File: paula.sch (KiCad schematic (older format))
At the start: 79 parts, among them CN200 DB9P RIGHT(1), CN201 DB9P LEFT(0), CN204 RIGHT AUDIO, CN205 LEFT AUDIO, J200 Conn_01x03_Male, Q200 MPF102, Q201 MPF102, Q202 2N3906, U200 PAULA, U202 74LS157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

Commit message: Makes the DRC happy
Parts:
- EMI230, EMI231, EMI232, EMI233, EMI234, EMI235, EMI236, EMI237, EMI238, EMI239, EMI240, EMI241, EMI242, EMI243: footprint Connector_PinSocket_2.54mm:PinSocket_1x03_P2.54mm_Vertical -> d_amiga:EMI_FILTER
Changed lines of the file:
@@
 F 0 "EMI231" H 6450 7600 50  0000 C CNN
 F 1 "C_Feedthrough" H 6350 7814 50  0001 C CNN
-F 2 "Connector_PinSocket_2.54mm:PinSocket_1x03_P2.54mm_Vertical" V 6350 7600 50  0001 C CNN
+F 2 "d_amiga:EMI_FILTER" V 6350 7600 50  0001 C CNN
 F 3 "~" V 6350 7600 50  0001 C CNN
 	1    6350 7600
@@
 F 0 "EMI232" H 6800 7800 50  0000 C CNN
 F 1 "C_Feedthrough" H 6700 8014 50  0001 C CNN
-F 2 "Connector_PinSocket_2.54mm:PinSocket_1x03_P2.54mm_Vertical" V 6700 7800 50  0001 C CNN
+F 2 "d_amiga:EMI_FILTER" V 6700 7800 50  0001 C CNN
 F 3 "~" V 6700 7800 50  0001 C CNN
 	1    6700 7800
@@
 F 0 "EMI233" H 7200 8000 50  0000 C CNN
 F 1 "C_Feedthrough" H 7100 8214 50  0001 C CNN
-F 2 "Connector_PinSocket_2.54mm:PinSocket_1x03_P2.54mm_Vertical" V 7100 8000 50  0001 C CNN
+F 2 "d_amiga:EMI_FILTER" V 7100 8000 50  0001 C CNN
 F 3 "~" V 7100 8000 50  0001 C CNN
 	1    7100 8000
@@
 F 0 "EMI230" H 6050 7400 50  0000 C CNN
 F 1 "C_Feedthrough" H 5950 7614 50  0001 C CNN
-F 2 "Connector_PinSocket_2.54mm:PinSocket_1x03_P2.54mm_Vertical" V 5950 7400 50  0001 C CNN
+F 2 "d_amiga:EMI_FILTER" V 5950 7400 50  0001 C CNN
 F 3 "~" V 5950 7400 50  0001 C CNN
 	1    5950 7400
@@
 F 0 "EMI234" H 6050 9600 50  0000 C CNN
 F 1 "C_Feedthrough" H 5950 9814 50  0001 C CNN
-F 2 "Connector_PinSocket_2.54mm:PinSocket_1x03_P2.54mm_Vertical" V 5950 9600 50  0001 C CNN
+F 2 "d_amiga:EMI_FILTER" V 5950 9600 50  0001 C CNN
 F 3 "~" V 5950 9600 50  0001 C CNN
 	1    5950 9600
@@
 F 0 "EMI235" H 6450 9800 50  0000 C CNN
 F 1 "C_Feedthrough" H 6350 10014 50  0001 C CNN
-F 2 "Connector_PinSocket_2.54mm:PinSocket_1x03_P2.54mm_Vertical" V 6350 9800 50  0001 C CNN
+F 2 "d_amiga:EMI_FILTER" V 6350 9800 50  0001 C CNN
 F 3 "~" V 6350 9800 50  0001 C CNN
 	1    6350 9800
@@
 F 0 "EMI236" H 6850 10000 50  0000 C CNN
 F 1 "C_Feedthrough" H 6750 10214 50  0001 C CNN
-F 2 "Connector_PinSocket_2.54mm:PinSocket_1x03_P2.54mm_Vertical" V 6750 10000 50  0001 C CNN
+F 2 "d_amiga:EMI_FILTER" V 6750 10000 50  0001 C CNN
 F 3 "~" V 6750 10000 50  0001 C CNN
 	1    6750 10000
@@
 F 0 "EMI237" H 7250 10200 50  0000 C CNN
 F 1 "C_Feedthrough" H 7150 10414 50  0001 C CNN
-F 2 "Connector_PinSocket_2.54mm:PinSocket_1x03_P2.54mm_Vertical" V 7150 10200 50  0001 C CNN
+F 2 "d_amiga:EMI_FILTER" V 7150 10200 50  0001 C CNN
 F 3 "~" V 7150 10200 50  0001 C CNN
 	1    7150 10200
@@
 F 0 "EMI238" H 9300 7100 50  0000 C CNN
 F 1 "C_Feedthrough" H 9200 7314 50  0001 C CNN
-F 2 "Connector_PinSocket_2.54mm:PinSocket_1x03_P2.54mm_Vertical" V 9200 7100 50  0001 C CNN
+F 2 "d_amiga:EMI_FILTER" V 9200 7100 50  0001 C CNN
 F 3 "~" V 9200 7100 50  0001 C CNN
 	1    9200 7100
@@
 F 0 "EMI239" H 9300 8400 50  0000 C CNN
 F 1 "C_Feedthrough" H 9200 8614 50  0001 C CNN
-F 2 "Connector_PinSocket_2.54mm:PinSocket_1x03_P2.54mm_Vertical" V 9200 8400 50  0001 C CNN
+F 2 "d_amiga:EMI_FILTER" V 9200 8400 50  0001 C CNN
 F 3 "~" V 9200 8400 50  0001 C CNN
 	1    9200 8400
@@
 F 0 "EMI240" H 9300 8750 50  0000 C CNN
 F 1 "C_Feedthrough" H 9200 8964 50  0001 C CNN
-F 2 "Connector_PinSocket_2.54mm:PinSocket_1x03_P2.54mm_Vertical" V 9200 8750 50  0001 C CNN
+F 2 "d_amiga:EMI_FILTER" V 9200 8750 50  0001 C CNN
 F 3 "~" V 9200 8750 50  0001 C CNN
 	1    9200 8750
@@
 F 0 "EMI241" H 9300 9350 50  0000 C CNN
 F 1 "C_Feedthrough" H 9200 9564 50  0001 C CNN
-F 2 "Connector_PinSocket_2.54mm:PinSocket_1x03_P2.54mm_Vertical" V 9200 9350 50  0001 C CNN
+F 2 "d_amiga:EMI_FILTER" V 9200 9350 50  0001 C CNN
 F 3 "~" V 9200 9350 50  0001 C CNN
 	1    9200 9350
@@
 F 0 "EMI242" H 9300 10600 50  0000 C CNN
 F 1 "C_Feedthrough" H 9200 10814 50  0001 C CNN
-F 2 "Connector_PinSocket_2.54mm:PinSocket_1x03_P2.54mm_Vertical" V 9200 10600 50  0001 C CNN
+F 2 "d_amiga:EMI_FILTER" V 9200 10600 50  0001 C CNN
 F 3 "~" V 9200 10600 50  0001 C CNN
 	1    9200 10600
@@
 F 0 "EMI243" H 9300 10900 50  0000 C CNN
 F 1 "C_Feedthrough" H 9200 11114 50  0001 C CNN
-F 2 "Connector_PinSocket_2.54mm:PinSocket_1x03_P2.54mm_Vertical" V 9200 10900 50  0001 C CNN
+F 2 "d_amiga:EMI_FILTER" V 9200 10900 50  0001 C CNN
 F 3 "~" V 9200 10900 50  0001 C CNN
 	1    9200 10900

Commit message: Add DoNotPopulate field for components which shouldn't be fitted
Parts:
- C230, C240: DoNotPopulate (none) -> yes
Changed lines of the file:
@@
 F 2 "Capacitor_THT:C_Rect_L11.5mm_W2.0mm_P10.00mm_MKT" H 6588 1200 50  0001 C CNN
 F 3 "~" H 6550 1350 50  0001 C CNN
+F 4 "yes" H 6550 1350 50  0001 C CNN "DoNotPopulate"
 	1    6550 1350
 	1    0    0    -1
@@
 F 2 "Capacitor_THT:C_Rect_L11.5mm_W2.0mm_P10.00mm_MKT" H 6588 3350 50  0001 C CNN
 F 3 "~" H 6550 3500 50  0001 C CNN
+F 4 "yes" H 6550 3500 50  0001 C CNN "DoNotPopulate"
 	1    6550 3500
 	1    0    0    -1

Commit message: Switch footprints for suitable modern replacements
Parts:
- C200, C202, C210, C211, C212, C213, C218, C230, C231, C232, C234, C240, C241, C242, C244, C900, C901: footprint Capacitor_THT:C_Rect_L11.5mm_W2.0mm_P10.00mm_MKT -> Capacitor_THT:C_Rect_L11.5mm_W2.6mm_P10.00mm_MKT
- C219, C220, C221: footprint Capacitor_THT:C_Rect_L11.5mm_W2.0mm_P10.00mm_MKT -> Capacitor_THT:C_Rect_L11.5mm_W4.0mm_P10.00mm_MKT
- C224: footprint Capacitor_THT:CP_Radial_D8.0mm_P5.00mm -> Capacitor_THT:CP_Radial_D5.0mm_P2.50mm
- C225: value 470uF 16v -> 470uF 16/25v
- C233: footprint Capacitor_THT:CP_Radial_D6.3mm_P2.50mm -> Capacitor_THT:CP_Radial_D8.0mm_P5.00mm
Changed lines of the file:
@@
 P 2750 750
 F 0 "C225" V 2900 700 50  0000 C CNN
-F 1 "470uF 16v" V 2800 500 50  0000 C CNN
+F 1 "470uF 16/25v" V 2800 500 50  0000 C CNN
 F 2 "Capacitor_THT:CP_Radial_D10.0mm_P5.00mm" H 2788 600 50  0001 C CNN
 F 3 "~" H 2750 750 50  0001 C CNN
@@
 F 0 "C200" V 2350 950 50  0000 C CNN
 F 1 "0.1uF" V 2650 950 50  0000 C CNN
-F 2 "Capacitor_THT:C_Rect_L11.5mm_W2.0mm_P10.00mm_MKT" H 2538 800 50  0001 C CNN
+F 2 "Capacitor_THT:C_Rect_L11.5mm_W2.6mm_P10.00mm_MKT" H 2538 800 50  0001 C CNN
 F 3 "~" H 2500 950 50  0001 C CNN
 	1    2500 950
@@
 F 0 "C210" H 3915 6046 50  0000 L CNN
 F 1 "0.047uF" H 3915 5955 50  0000 L CNN
-F 2 "Capacitor_THT:C_Rect_L11.5mm_W2.0mm_P10.00mm_MKT" H 3838 5850 50  0001 C CNN
+F 2 "Capacitor_THT:C_Rect_L11.5mm_W2.6mm_P10.00mm_MKT" H 3838 5850 50  0001 C CNN
 F 3 "~" H 3800 6000 50  0001 C CNN
 	1    3800 6000
@@
 F 0 "C211" H 4465 6046 50  0000 L CNN
 F 1 "0.047uF" H 4465 5955 50  0000 L CNN
-F 2 "Capacitor_THT:C_Rect_L11.5mm_W2.0mm_P10.00mm_MKT" H 4388 5850 50  0001 C CNN
+F 2 "Capacitor_THT:C_Rect_L11.5mm_W2.6mm_P10.00mm_MKT" H 4388 5850 50  0001 C CNN
 F 3 "~" H 4350 6000 50  0001 C CNN
 	1    4350 6000
@@
 F 0 "C212" H 5015 6046 50  0000 L CNN
 F 1 "0.047uF" H 5015 5955 50  0000 L CNN
-F 2 "Capacitor_THT:C_Rect_L11.5mm_W2.0mm_P10.00mm_MKT" H 4938 5850 50  0001 C CNN
+F 2 "Capacitor_THT:C_Rect_L11.5mm_W2.6mm_P10.00mm_MKT" H 4938 5850 50  0001 C CNN
 F 3 "~" H 4900 6000 50  0001 C CNN
 	1    4900 6000
@@
 F 0 "C213" H 5565 6046 50  0000 L CNN
 F 1 "0.047uF" H 5565 5955 50  0000 L CNN
-F 2 "Capacitor_THT:C_Rect_L11.5mm_W2.0mm_P10.00mm_MKT" H 5488 5850 50  0001 C CNN
+F 2 "Capacitor_THT:C_Rect_L11.5mm_W2.6mm_P10.00mm_MKT" H 5488 5850 50  0001 C CNN
 F 3 "~" H 5450 6000 50  0001 C CNN
 	1    5450 6000
@@
 F 0 "C218" V 6721 6750 50  0000 C CNN
 F 1 "0.047uF" V 6812 6750 50  0000 C CNN
-F 2 "Capacitor_THT:C_Rect_L11.5mm_W2.0mm_P10.00mm_MKT" H 6950 6750 50  0001 C CNN
+F 2 "Capacitor_THT:C_Rect_L11.5mm_W2.6mm_P10.00mm_MKT" H 6950 6750 50  0001 C CNN
 F 3 "~" H 6950 6750 50  0001 C CNN
 	1    6950 6750
@@
 F 0 "C202" H 3315 8646 50  0000 L CNN
 F 1 "0.1uF" H 3315 8555 50  0000 L CNN
-F 2 "Capacitor_THT:C_Rect_L11.5mm_W2.0mm_P10.00mm_MKT" H 3238 8450 50  0001 C CNN
+F 2 "Capacitor_THT:C_Rect_L11.5mm_W2.6mm_P10.00mm_MKT" H 3238 8450 50  0001 C CNN
 F 3 "~" H 3200 8600 50  0001 C CNN
 	1    3200 8600
@@
 F 0 "C220" H 10715 7346 50  0000 L CNN
 F 1 "0.22uF" H 10715 7255 50  0000 L CNN
-F 2 "Capacitor_THT:C_Rect_L11.5mm_W2.0mm_P10.00mm_MKT" H 10638 7150 50  0001 C CNN
+F 2 "Capacitor_THT:C_Rect_L11.5mm_W4.0mm_P10.00mm_MKT" H 10638 7150 50  0001 C CNN
 F 3 "~" H 10600 7300 50  0001 C CNN
 	1    10600 7300
@@
 F 0 "C221" H 10715 7846 50  0000 L CNN
 F 1 "0.22uF" H 10715 7755 50  0000 L CNN
-F 2 "Capacitor_THT:C_Rect_L11.5mm_W2.0mm_P10.00mm_MKT" H 10638 7650 50  0001 C CNN
+F 2 "Capacitor_THT:C_Rect_L11.5mm_W4.0mm_P10.00mm_MKT" H 10638 7650 50  0001 C CNN
 F 3 "~" H 10600 7800 50  0001 C CNN
 	1    10600 7800
@@
 F 0 "C240" H 6665 1396 50  0000 L CNN
 F 1 "0.1uF" H 6665 1305 50  0000 L CNN
-F 2 "Capacitor_THT:C_Rect_L11.5mm_W2.0mm_P10.00mm_MKT" H 6588 1200 50  0001 C CNN
+F 2 "Capacitor_THT:C_Rect_L11.5mm_W2.6mm_P10.00mm_MKT" H 6588 1200 50  0001 C CNN
 F 3 "~" H 6550 1350 50  0001 C CNN
 F 4 "yes" H 6550 1350 50  0001 C CNN "DoNotPopulate"
@@
 F 0 "C241" H 8465 1196 50  0000 L CNN
 F 1 "6800pF" H 8465 1105 50  0000 L CNN
-F 2 "Capacitor_THT:C_Rect_L11.5mm_W2.0mm_P10.00mm_MKT" H 8388 1000 50  0001 C CNN
+F 2 "Capacitor_THT:C_Rect_L11.5mm_W2.6mm_P10.00mm_MKT" H 8388 1000 50  0001 C CNN
 F 3 "~" H 8350 1150 50  0001 C CNN
 	1    8350 1150
@@
 F 0 "C242" H 9915 1846 50  0000 L CNN
 F 1 "3900pF" H 9915 1755 50  0000 L CNN
-F 2 "Capacitor_THT:C_Rect_L11.5mm_W2.0mm_P10.00mm_MKT" H 9838 1650 50  0001 C CNN
+F 2 "Capacitor_THT:C_Rect_L11.5mm_W2.6mm_P10.00mm_MKT" H 9838 1650 50  0001 C CNN
 F 3 "~" H 9800 1800 50  0001 C CNN
 	1    9800 1800
@@
 F 0 "C244" H 13615 1996 50  0000 L CNN
 F 1 "0.1uF" H 13615 1905 50  0000 L CNN
-F 2 "Capacitor_THT:C_Rect_L11.5mm_W2.0mm_P10.00mm_MKT" H 13538 1800 50  0001 C CNN
+F 2 "Capacitor_THT:C_Rect_L11.5mm_W2.6mm_P10.00mm_MKT" H 13538 1800 50  0001 C CNN
 F 3 "~" H 13500 1950 50  0001 C CNN
 	1    13500 1950
@@
 F 0 "C230" H 6665 3546 50  0000 L CNN
 F 1 "0.1uF" H 6665 3455 50  0000 L CNN
-F 2 "Capacitor_THT:C_Rect_L11.5mm_W2.0mm_P10.00mm_MKT" H 6588 3350 50  0001 C CNN
+F 2 "Capacitor_THT:C_Rect_L11.5mm_W2.6mm_P10.00mm_MKT" H 6588 3350 50  0001 C CNN
 F 3 "~" H 6550 3500 50  0001 C CNN
 F 4 "yes" H 6550 3500 50  0001 C CNN "DoNotPopulate"
@@
 F 0 "C231" H 8465 3346 50  0000 L CNN
 F 1 "6800pF" H 8465 3255 50  0000 L CNN
-F 2 "Capacitor_THT:C_Rect_L11.5mm_W2.0mm_P10.00mm_MKT" H 8388 3150 50  0001 C CNN
+F 2 "Capacitor_THT:C_Rect_L11.5mm_W2.6mm_P10.00mm_MKT" H 8388 3150 50  0001 C CNN
 F 3 "~" H 8350 3300 50  0001 C CNN
 	1    8350 3300
@@
 F 0 "C232" H 9915 3996 50  0000 L CNN
 F 1 "3900pF" H 9915 3905 50  0000 L CNN
-F 2 "Capacitor_THT:C_Rect_L11.5mm_W2.0mm_P10.00mm_MKT" H 9838 3800 50  0001 C CNN
+F 2 "Capacitor_THT:C_Rect_L11.5mm_W2.6mm_P10.00mm_MKT" H 9838 3800 50  0001 C CNN
 F 3 "~" H 9800 3950 50  0001 C CNN
 	1    9800 3950
@@
 F 0 "C233" V 12205 3850 50  0000 C CNN
 F 1 "22uF 16V" V 12114 3850 50  0000 C CNN
-F 2 "Capacitor_THT:CP_Radial_D6.3mm_P2.50mm" H 11988 3700 50  0001 C CNN
+F 2 "Capacitor_THT:CP_Radial_D8.0mm_P5.00mm" H 11988 3700 50  0001 C CNN
 F 3 "~" H 11950 3850 50  0001 C CNN
 	1    11950 3850
@@
 F 0 "C234" H 13615 4146 50  0000 L CNN
 F 1 "0.1uF" H 13615 4055 50  0000 L CNN
-F 2 "Capacitor_THT:C_Rect_L11.5mm_W2.0mm_P10.00mm_MKT" H 13538 3950 50  0001 C CNN
+F 2 "Capacitor_THT:C_Rect_L11.5mm_W2.6mm_P10.00mm_MKT" H 13538 3950 50  0001 C CNN
 F 3 "~" H 13500 4100 50  0001 C CNN
 	1    13500 4100
@@
 F 0 "C219" H 14015 8996 50  0000 L CNN
 F 1 "0.22uF" H 14015 8905 50  0000 L CNN
-F 2 "Capacitor_THT:C_Rect_L11.5mm_W2.0mm_P10.00mm_MKT" H 13938 8800 50  0001 C CNN
+F 2 "Capacitor_THT:C_Rect_L11.5mm_W4.0mm_P10.00mm_MKT" H 13938 8800 50  0001 C CNN
 F 3 "~" H 13900 8950 50  0001 C CNN
 	1    13900 8950
@@
 F 0 "C224" H 14568 8996 50  0000 L CNN
 F 1 "4.7uF 16V" H 14568 8905 50  0000 L CNN
-F 2 "Capacitor_THT:CP_Radial_D8.0mm_P5.00mm" H 14488 8800 50  0001 C CNN
+F 2 "Capacitor_THT:CP_Radial_D5.0mm_P2.50mm" H 14488 8800 50  0001 C CNN
 F 3 "~" H 14450 8950 50  0001 C CNN
 	1    14450 8950
@@
 F 0 "C900" H 12965 7346 50  0000 L CNN
 F 1 "0.1uF" H 12965 7255 50  0000 L CNN
-F 2 "Capacitor_THT:C_Rect_L11.5mm_W2.0mm_P10.00mm_MKT" H 12888 7150 50  0001 C CNN
+F 2 "Capacitor_THT:C_Rect_L11.5mm_W2.6mm_P10.00mm_MKT" H 12888 7150 50  0001 C CNN
 F 3 "~" H 12850 7300 50  0001 C CNN
 	1    12850 7300
@@
 F 0 "C901" H 12965 7846 50  0000 L CNN
 F 1 "0.1uF" H 12965 7755 50  0000 L CNN
-F 2 "Capacitor_THT:C_Rect_L11.5mm_W2.0mm_P10.00mm_MKT" H 12888 7650 50  0001 C CNN
+F 2 "Capacitor_THT:C_Rect_L11.5mm_W2.6mm_P10.00mm_MKT" H 12888 7650 50  0001 C CNN
 F 3 "~" H 12850 7800 50  0001 C CNN
 	1    12850 7800

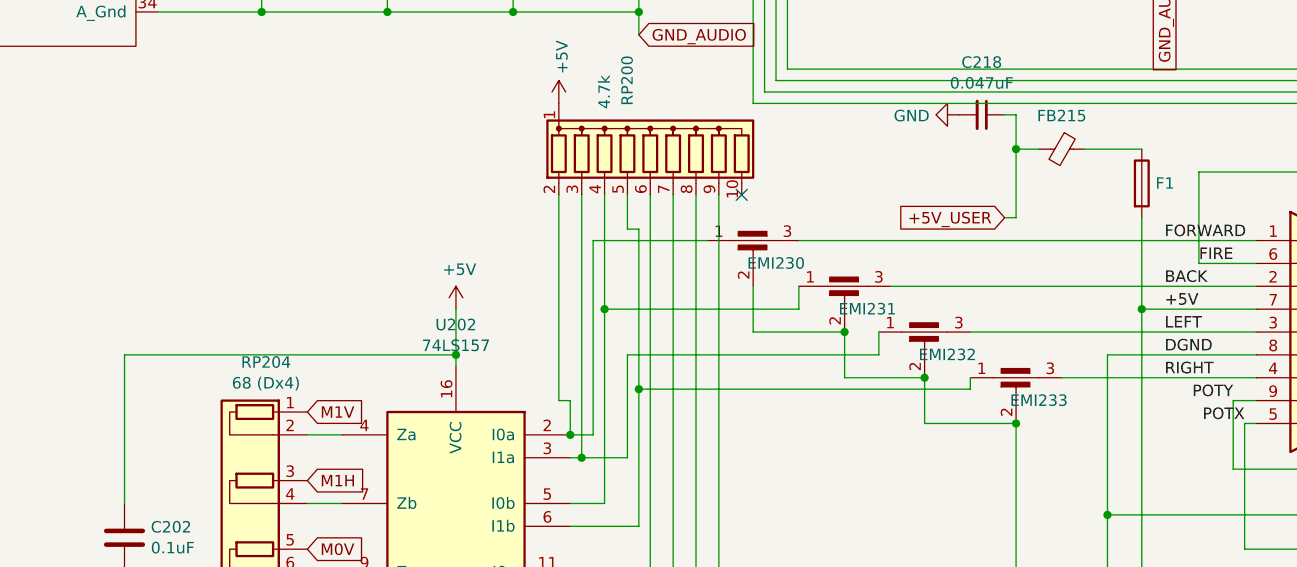
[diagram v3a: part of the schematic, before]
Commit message: Some footprints updates; Add all Mouser references
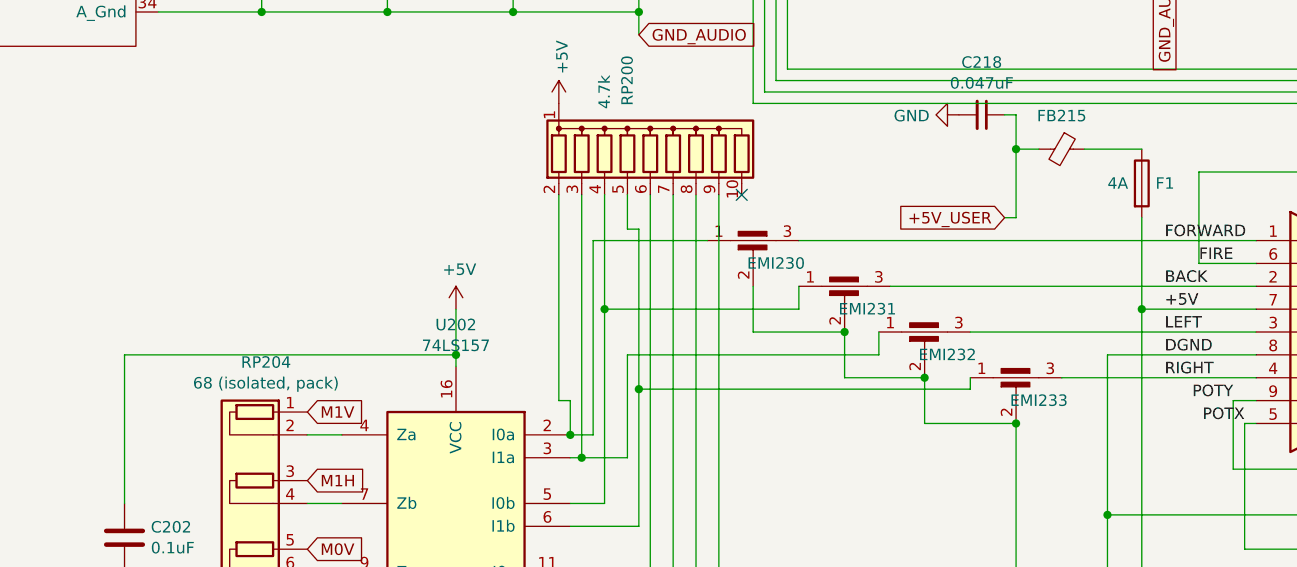
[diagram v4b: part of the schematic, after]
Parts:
- C200, C202, C230, C234, C240, C244, C900, C901: RefOrder (none) -> 581-SA105C104KARC
- C204: RefOrder (none) -> 581-SA105C103K
- C210, C211, C212, C213, C218: RefOrder (none) -> 581-SA105C473KARC
- C219, C220, C221: RefOrder (none) -> 594-A224K20X7RF5TAA
- C222, C223: RefOrder (none) -> 667-ECA-1CM470B
- C224: RefOrder (none) -> 647-UMA1C4R7MCD2TP
- C225: RefOrder (none) -> 647-UVR1E471MPD
- C231, C241: RefOrder (none) -> 581-SA101C682MAA
- C232, C242: RefOrder (none) -> 581-SA051C392KAA
- C233, C243: RefOrder (none) -> 667-ECA-1CM220B
- EMI230, EMI231, EMI232, EMI233, EMI234, EMI235, EMI236, EMI237, EMI238, EMI239, EMI240, EMI241, EMI242, EMI243: value C_Feedthrough -> 6.8nF (Type F 682); RefOrder (none) -> 81-DSS1NB32A682Q91A
- F1: value Fuse -> 4A; RefOrder (none) -> 576-0251004.MRT1L
- FB215, FB401: RefOrder (none) -> 875-28L0138-10R-10
- Q200, Q201: RefOrder (none) -> 610-2N3906 or 512-J113D74Z
- Q202: RefOrder (none) -> 833-2N3906-AP
- R200: RefOrder (none) -> 603-CFR-25JR-52-1R
- R202, R206, R214, R231, R232, R241, R242: RefOrder (none) -> 603-CFR-25JR-5210K
- R204, R205: RefOrder (none) -> 603-CFR-25JR-52470K
- R207, R208: RefOrder (none) -> 603-CFR-25JB-52-10R
- R209, R210: RefOrder (none) -> 603-CFR-25JT-52-1K2
- R213: RefOrder (none) -> 603-CFR-25JR-522K7
- R230, R240: RefOrder (none) -> 603-CFR-25JB-52-360R
- R233, R243, R900: RefOrder (none) -> 603-CFR-25JR-521K
- R234, R244: RefOrder (none) -> 603-CFR-25JR-52390R
- RP200: RefOrder (none) -> 858-L101S472LF
- RP204: value 68 (Dx4) -> 68 (isolated, pack); RefOrder (none) -> 858-L083S680LF
- U202: RefOrder (none) -> 595-SN74LS157N
- U204: RefOrder (none) -> 926-LF347N/NOPB

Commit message: Got the components, reduce some footprints
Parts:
- C204: footprint Capacitor_THT:C_Rect_L11.5mm_W2.0mm_P10.00mm_MKT -> Capacitor_THT:C_Rect_L11.5mm_W2.6mm_P10.00mm_MKT
- C219, C220, C221: footprint Capacitor_THT:C_Rect_L11.5mm_W4.0mm_P10.00mm_MKT -> Capacitor_THT:C_Rect_L11.5mm_W2.6mm_P10.00mm_MKT
- C222, C223: footprint Capacitor_THT:CP_Radial_D8.0mm_P5.00mm -> Capacitor_THT:CP_Radial_Tantal_D5.5mm_P5.00mm
- C233, C243: footprint Capacitor_THT:CP_Radial_D8.0mm_P5.00mm -> Capacitor_THT:CP_Radial_Tantal_D5.0mm_P5.00mm
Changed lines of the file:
@@
 F 0 "C222" H 11268 7346 50  0000 L CNN
 F 1 "47uF 16V" H 11268 7255 50  0000 L CNN
-F 2 "Capacitor_THT:CP_Radial_D8.0mm_P5.00mm" H 11188 7150 50  0001 C CNN
+F 2 "Capacitor_THT:CP_Radial_Tantal_D5.5mm_P5.00mm" H 11188 7150 50  0001 C CNN
 F 3 "~" H 11150 7300 50  0001 C CNN
 F 4 "667-ECA-1CM470B" H 11150 7300 50  0001 C CNN "RefOrder"
@@
 F 0 "C223" H 11268 7846 50  0000 L CNN
 F 1 "47uF 16V" H 11268 7755 50  0000 L CNN
-F 2 "Capacitor_THT:CP_Radial_D8.0mm_P5.00mm" H 11188 7650 50  0001 C CNN
+F 2 "Capacitor_THT:CP_Radial_Tantal_D5.5mm_P5.00mm" H 11188 7650 50  0001 C CNN
 F 3 "~" H 11150 7800 50  0001 C CNN
 F 4 "667-ECA-1CM470B" H 11150 7800 50  0001 C CNN "RefOrder"
@@
 F 0 "C220" H 10715 7346 50  0000 L CNN
 F 1 "0.22uF" H 10715 7255 50  0000 L CNN
-F 2 "Capacitor_THT:C_Rect_L11.5mm_W4.0mm_P10.00mm_MKT" H 10638 7150 50  0001 C CNN
+F 2 "Capacitor_THT:C_Rect_L11.5mm_W2.6mm_P10.00mm_MKT" H 10638 7150 50  0001 C CNN
 F 3 "~" H 10600 7300 50  0001 C CNN
 F 4 "594-A224K20X7RF5TAA" H 10600 7300 50  0001 C CNN "RefOrder"
@@
 F 0 "C221" H 10715 7846 50  0000 L CNN
 F 1 "0.22uF" H 10715 7755 50  0000 L CNN
-F 2 "Capacitor_THT:C_Rect_L11.5mm_W4.0mm_P10.00mm_MKT" H 10638 7650 50  0001 C CNN
+F 2 "Capacitor_THT:C_Rect_L11.5mm_W2.6mm_P10.00mm_MKT" H 10638 7650 50  0001 C CNN
 F 3 "~" H 10600 7800 50  0001 C CNN
 F 4 "594-A224K20X7RF5TAA" H 10600 7800 50  0001 C CNN "RefOrder"
@@
 F 0 "C243" V 12205 1700 50  0000 C CNN
 F 1 "22uF 16V" V 12114 1700 50  0000 C CNN
-F 2 "Capacitor_THT:CP_Radial_D8.0mm_P5.00mm" H 11988 1550 50  0001 C CNN
+F 2 "Capacitor_THT:CP_Radial_Tantal_D5.0mm_P5.00mm" H 11988 1550 50  0001 C CNN
 F 3 "~" H 11950 1700 50  0001 C CNN
 F 4 "667-ECA-1CM220B" H 11950 1700 50  0001 C CNN "RefOrder"
@@
 F 0 "C233" V 12205 3850 50  0000 C CNN
 F 1 "22uF 16V" V 12114 3850 50  0000 C CNN
-F 2 "Capacitor_THT:CP_Radial_D8.0mm_P5.00mm" H 11988 3700 50  0001 C CNN
+F 2 "Capacitor_THT:CP_Radial_Tantal_D5.0mm_P5.00mm" H 11988 3700 50  0001 C CNN
 F 3 "~" H 11950 3850 50  0001 C CNN
 F 4 "667-ECA-1CM220B" H 11950 3850 50  0001 C CNN "RefOrder"
@@
 F 0 "C204" H 7865 5946 50  0000 L CNN
 F 1 "0.01uF" H 7865 5855 50  0000 L CNN
-F 2 "Capacitor_THT:C_Rect_L11.5mm_W2.0mm_P10.00mm_MKT" H 7788 5750 50  0001 C CNN
+F 2 "Capacitor_THT:C_Rect_L11.5mm_W2.6mm_P10.00mm_MKT" H 7788 5750 50  0001 C CNN
 F 3 "~" H 7750 5900 50  0001 C CNN
 F 4 "581-SA105C103K" H 7750 5900 50  0001 C CNN "RefOrder"
@@
 F 0 "C219" H 14015 8996 50  0000 L CNN
 F 1 "0.22uF" H 14015 8905 50  0000 L CNN
-F 2 "Capacitor_THT:C_Rect_L11.5mm_W4.0mm_P10.00mm_MKT" H 13938 8800 50  0001 C CNN
+F 2 "Capacitor_THT:C_Rect_L11.5mm_W2.6mm_P10.00mm_MKT" H 13938 8800 50  0001 C CNN
 F 3 "~" H 13900 8950 50  0001 C CNN
 F 4 "594-A224K20X7RF5TAA" H 13900 8950 50  0001 C CNN "RefOrder"
